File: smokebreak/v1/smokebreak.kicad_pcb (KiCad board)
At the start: 6 copper layers, 94 x 52 mm, 204 parts, among them J1 XT60 male, J10 JST-XH 4S, J11 JST-XH 3S, J12 JST-XH 2S, J2 XT30 male, J3 XT60 female lead, J4 XT30 female lead, J5 JST-XH 6S, J6 SWD, J7 TFT1901 FPC, J8 USB-C, J9 JST-XH 5S, Q1 input FET, Q10 BC817, Q11 BSC070N10LS5, Q2 output FET, Q3 SUD50P10-43L, Q4 MMBTA42, Q5 BC817, Q6 MMBT5401, Q7 MMBT5401, Q8 2N7002, Q9 AO3400A, SW1 ON-OFF-(ON), SW2 Limit -, SW3 Limit +, U1 TPS48000, U10 SN74AHCT1G125, U11 USBLC6-2SC6, U12 LMV331, U2 INA181A2, U3 LMR36506R5, U4 TLV75533, U5 STM32G0B1RBT6, U6 DRV5032FA, U7 74LVC1G11, U8 LMV331, U9 SN74LVC1G74

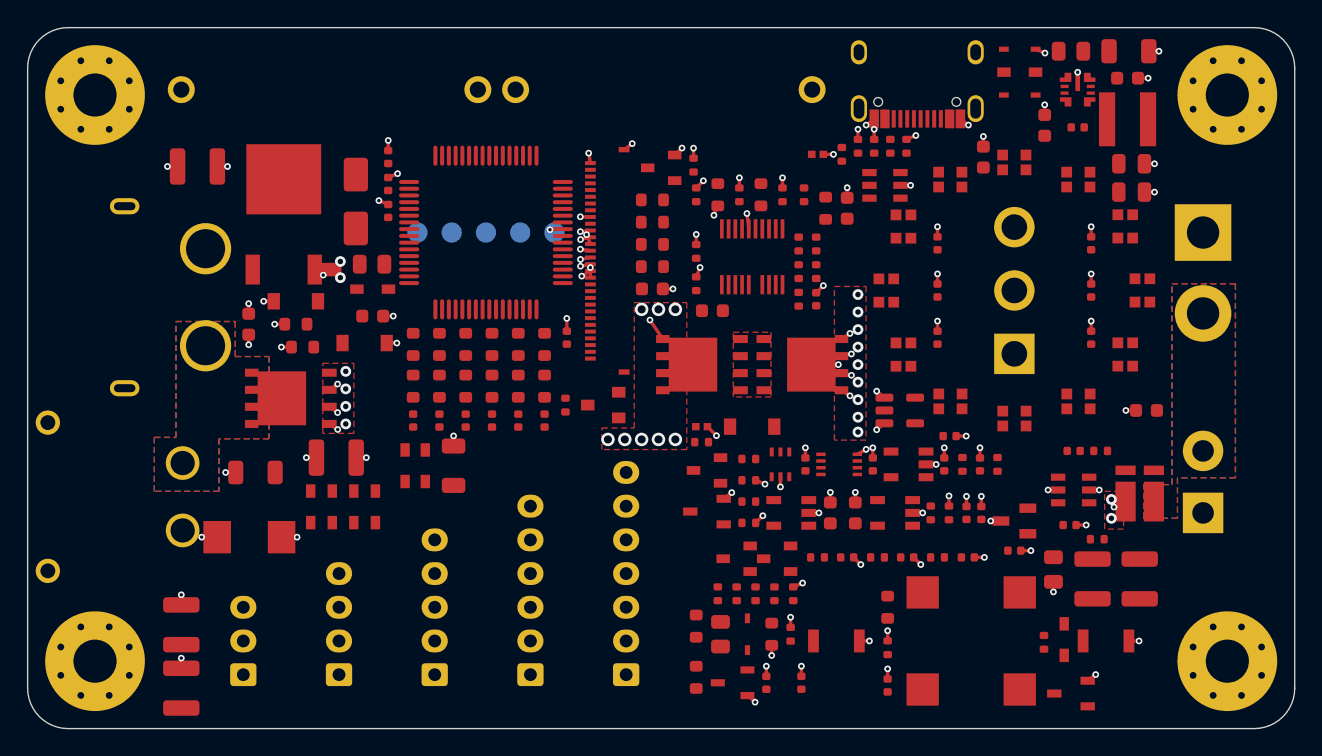
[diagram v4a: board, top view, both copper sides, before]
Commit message: Compact board: power copper for the compact layout (VBAT island for the XT30, fuse vias under its body, Q1/Q2 drain and source copper, drone and battery minus), 1 oz inner layers, tight-courtyard XH sockets, art fields; pre-route DRC clean
Co-Authored-By: Claude Opus 5.5 <noreply@anthropic.com>
Claude-Session: https://claude.ai/code/session_01SBnFJLvm1wBa1jZy4RXnma
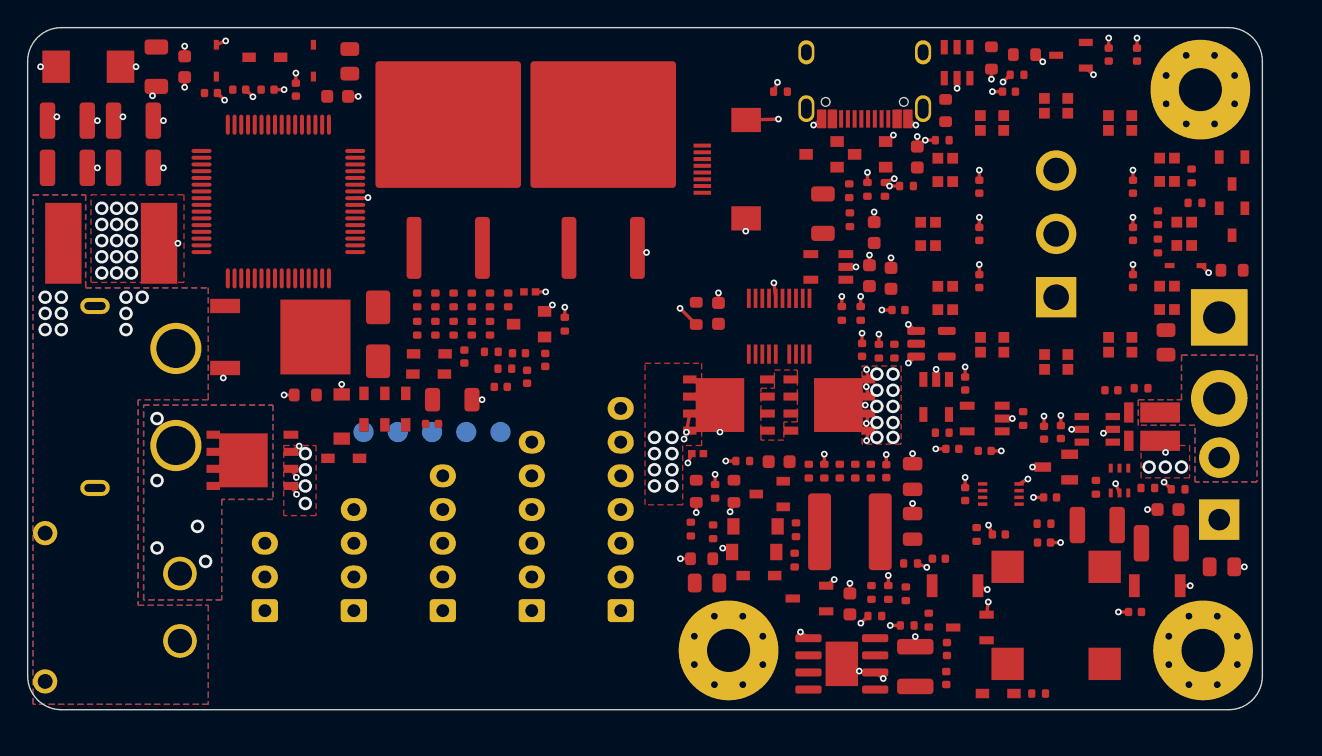
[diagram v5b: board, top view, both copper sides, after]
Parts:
- removed H4: M3, MountingHole_M3_Washer
- removed R57, R58, R59: 100 Ohm, R_0603_1608Metric
- removed the R_PRE at (122.4, 104.6)
- added C57: 56pF 50V, C_0402_1005Metric, F.Cu at (167.6, 139.4)
- added F1: 40 A 80 V, Fuse_Eaton_2822HC, F.Cu at (106.2, 116.0)
- added Q12: 2N7002, SOT-23_L2.9-W1.3-P1.90-LS2.4-BR, F.Cu at (162.5, 109.4)
- added R76: 30.9 k, R_0402_1005Metric, F.Cu at (165.2, 144.3)
- added R77: 453 k, R_0402_1005Metric, F.Cu at (165.2, 142.0)
- added R78: 143 k, R_0402_1005Metric, F.Cu at (165.5, 139.8)
- added R79: 100 k, R_0402_1005Metric, F.Cu at (166.8, 143.9)
- added R80: 100 k, R_0402_1005Metric, F.Cu at (160.9, 112.1)
- added R_PRE: 3.9 Ohm 20 W, TO-263-2, F.Cu at (131.2, 108.7)
- C26: value 1uF 100V -> 2u2F 100V; footprint C_1206_3216Metric -> C_1210_3225Metric
- C28: value 1uF 25V -> 3n3F 50V; footprint C_0603_1608Metric -> C_0402_1005Metric
- C29: value 100nF 16V -> 2n2F 50V
- J10: footprint JST_XH_B5B-XH-A_1x05_P2.50mm_Vertical -> JST_XH_B5B-XH-A_1x05_P2.50mm_Vertical_Tight
- J11: footprint JST_XH_B4B-XH-A_1x04_P2.50mm_Vertical -> JST_XH_B4B-XH-A_1x04_P2.50mm_Vertical_Tight
- J12: footprint JST_XH_B3B-XH-A_1x03_P2.50mm_Vertical -> JST_XH_B3B-XH-A_1x03_P2.50mm_Vertical_Tight
- J3: footprint WirePads_12AWG -> WirePads_12AWG_NS
- J4: footprint WirePads_16AWG -> WirePads_16AWG_NS
- J5: footprint JST_XH_B7B-XH-A_1x07_P2.50mm_Vertical -> JST_XH_B7B-XH-A_1x07_P2.50mm_Vertical_Tight
- J7: value TFT1901 FPC -> ER-TFT2.25-1 FPC; footprint FFC-SMD_30P-P0.50_FH34SRJ-30S-0.5SH -> Hirose_FH12-8S-0.5SH_1x08-1MP_P0.50mm_Horizontal
- J9: footprint JST_XH_B6B-XH-A_1x06_P2.50mm_Vertical -> JST_XH_B6B-XH-A_1x06_P2.50mm_Vertical_Tight
- L1: footprint IND-SMD_L4.0-W4.0_SLS3DXX -> L_Changjiang_FNR6045S
- Q9: value AO3400A -> AO3401A; footprint SOT-23-3_L2.9-W1.3-P1.90-LS2.4-BR -> SOT-23_L2.9-W1.3-P1.90-LS2.4-BR
- R36, R37, R38, R39, R40, R41, R42, R43, R44, R45, R46, R47: footprint R_0603_1608Metric -> R_0402_1005Metric
- R5: value 18 k -> 19.6 k
- R56: value 100 Ohm -> 33 Ohm; footprint R_0603_1608Metric -> R_1206_3216Metric
- R_PRE2: value 3.9 Ohm 5 W -> 3.9 Ohm 20 W; footprint RES-TH_BD7.5-L18.0-P22.00-D1.0 -> TO-263-2
- U3: value LMR36506R5 -> LM5164DDAR; footprint VQFN-9_L2.1-W2.1-P0.50-TL -> SOIC-8-1EP_3.9x4.9mm_P1.27mm_EP2.41x3.3mm
- moved H1 82.0 mm to (187.0, 104.6)
- moved D14 59.6 mm to (114.0, 102.5), turned to 90 degrees
- moved D15 56.0 mm to (117.6, 102.2)
- moved R53 53.5 mm to (123.9, 102.5), turned to 90 degrees
- moved C16 53.1 mm to (180.2, 102.0)
- moved D5 52.9 mm to (177.4, 102.0)
- moved D16 52.5 mm to (121.2, 102.5), turned to 90 degrees
- moved R32 52.2 mm to (173.9, 102.0), turned to 180 degrees
- moved C17 50.3 mm to (182.3, 102.0)
- moved C26 48.3 mm to (165.8, 147.4), turned to 90 degrees
- moved R28 47.7 mm to (189.3, 118.0), turned to 180 degrees
- moved H3 47.0 mm to (152.0, 146.2)
- moved R72 46.9 mm to (186.3, 111.0)
- moved Q6 46.7 mm to (189.3, 110.6), turned to 90 degrees
- moved C15 46.5 mm to (172.8, 104.8), turned to 180 degrees
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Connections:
- C28 pad 1: BUCK_VCC -> BUCK_RA
- C28 pad 2: GND -> +5V
- D16 pad 1: AUX -> +5V
- J1 pad 2: VIN -> VBAT
- J2 pad 2: VIN -> VBAT
- J7 pad 1: GND -> LCD_LEDA
- J7 pad 2: +3V3 -> GND
- J7 pad 3: +3V3 -> LCD_RST
- J7 pad 4: +3V3 -> LCD_DC
- J7 pad 5: LCD_RST -> LCD_SDA
- J7 pad 6: LCD_CS -> LCD_SCK
- J7 pad 7: LCD_SCK -> +3V3
- J7 pad 8: LCD_DC -> LCD_CS
- Q9 pad 1: LCD_BL -> BL_G
- Q9 pad 2: GND -> +5V
- R56 pad 1: BL_K1 -> BL_SW
- R56 pad 2: BL_SW -> LCD_LEDA
- R_PRE2 pad 2: VOUT -> (no net)
- U3 pad 1: BUCK_VCC -> GND
- U3 pad 2: (no net) -> AUX_F
- U3 pad 4: AUX_F -> BUCK_RON
- U3 pad 5: BUCK_SW -> BUCK_FB
- U3 pad 6: BUCK_BOOT -> GND
- U3 pad 7: BUCK_VCC -> BUCK_BOOT
- U3 pad 8: +5V -> BUCK_SW
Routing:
- net VIN: track 11.8 -> 16.6 mm, vias 22 -> 40
- net VOUT: track 7.25 -> 9.50 mm, vias 17 -> 21
- net GND: track 75.9 -> 75.1 mm, vias 105 -> 102
- net VBAT: vias 0 -> 10
- net BATT_NEG: vias 0 -> 5
- added copper zone on B.Cu, net VBAT
- added copper zone on F.Cu, net VBAT
- added copper zone on In2.Cu, net VBAT
- added copper zone on In3.Cu, net VBAT
- added copper zone on In4.Cu, net VBAT
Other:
- board size 94 x 52 mm -> 91.6 x 50.6 mm
